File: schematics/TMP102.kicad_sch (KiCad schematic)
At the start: 7 parts, among them J9 Fan_CPU_4pin, U5 TMP102xxDRL

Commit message: Файлы измененный Kicad
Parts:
- C26, R15, R16: now not fitted; now left out of the parts list
- U4: renamed from U5; now not fitted; now left out of the parts list
- renumbered J9 to FAN0, R24 to R0400, R25 to R0401
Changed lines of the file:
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@@
 	(text "Address: 1001000x"
 		(exclude_from_sim no)
-		(at 107.95 105.918 0)
+		(at 102.108 108.204 0)
 		(effects
 			(font
-				(size 1.27 1.27)
+				(size 2.54 2.54)
 			)
 		)
@@
 	(text "Что-то из документации не понятно че там происходит.\nОдни пишут, что на выходе тахометра +7V, другие что 3.3V\nили вообще +12V. Одно понятно. Обычная понижайка справится"
 		(exclude_from_sim no)
-		(at 169.672 117.602 0)
+		(at 154.432 134.62 0)
 		(effects
 			(font
-				(size 1.27 1.27)
+				(size 2.54 2.54)
 			)
 			(justify left)
@@
 		(at 107.95 85.09 0)
 		(unit 1)
-		(exclude_from_sim no)
-		(in_bom yes)
-		(on_board yes)
-		(dnp no)
+		(exclude_from_sim yes)
+		(in_bom no)
+		(on_board no)
+		(dnp yes)
 		(fields_autoplaced yes)
 		(property "Reference" "R15"
@@
 		(at 135.89 101.6 0)
 		(unit 1)
-		(exclude_from_sim no)
-		(in_bom yes)
-		(on_board yes)
-		(dnp no)
-		(property "Reference" "U5"
+		(exclude_from_sim yes)
+		(in_bom no)
+		(on_board no)
+		(dnp yes)
+		(property "Reference" "U4"
 			(at 144.78 89.154 0)
 			(effects
@@
 			(project "MasterBoard"
 				(path "/97e8f341-b455-4614-ab7f-cc310164e7aa/c42b4888-b871-46c0-9d59-6fc9dc24c285"
-					(reference "U5")
+					(reference "U4")
 					(unit 1)
 				)
@@
 		(dnp no)
 		(fields_autoplaced yes)
-		(property "Reference" "R25"
+		(property "Reference" "R0401"
 			(at 199.39 104.1399 0)
 			(effects
@@
 			(project "MasterBoard"
 				(path "/97e8f341-b455-4614-ab7f-cc310164e7aa/c42b4888-b871-46c0-9d59-6fc9dc24c285"
-					(reference "R25")
+					(reference "R0401")
 					(unit 1)
 				)
@@
 		(on_board yes)
 		(dnp no)
-		(property "Reference" "J9"
-			(at 202.438 70.358 90)
+		(property "Reference" "FAN0"
+			(at 199.39 72.136 90)
 			(effects
 				(font
@@
 				)
 				(justify left)
+				(hide yes)
 			)
 		)
@@
 			(project "MasterBoard"
 				(path "/97e8f341-b455-4614-ab7f-cc310164e7aa/c42b4888-b871-46c0-9d59-6fc9dc24c285"
-					(reference "J9")
+					(reference "FAN0")
 					(unit 1)
 				)
@@
 		(dnp no)
 		(fields_autoplaced yes)
-		(property "Reference" "R24"
+		(property "Reference" "R0400"
 			(at 199.39 93.9799 0)
 			(effects
@@
 			(project "MasterBoard"
 				(path "/97e8f341-b455-4614-ab7f-cc310164e7aa/c42b4888-b871-46c0-9d59-6fc9dc24c285"
-					(reference "R24")
+					(reference "R0400")
 					(unit 1)
 				)
@@
 		(at 127 85.09 0)
 		(unit 1)
-		(exclude_from_sim no)
-		(in_bom yes)
-		(on_board yes)
-		(dnp no)
+		(exclude_from_sim yes)
+		(in_bom no)
+		(on_board no)
+		(dnp yes)
 		(fields_autoplaced yes)
 		(property "Reference" "C26"
@@
 		(at 118.11 85.09 0)
 		(unit 1)
-		(exclude_from_sim no)
-		(in_bom yes)
-		(on_board yes)
-		(dnp no)
+		(exclude_from_sim yes)
+		(in_bom no)
+		(on_board no)
+		(dnp yes)
 		(fields_autoplaced yes)
 		(property "Reference" "R16"

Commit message: Прошелся по всей схеме: 1. почистил компоненты; 2. задал посадочные места; 3. Выставил все ссылки на плате в притык, дальнейшее расширение - смена мк
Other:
- company: (none) -> Филимонов и К
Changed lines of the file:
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@@
 	(title_block
 		(date "2025-02-25")
+		(company "Филимонов и К")
 		(comment 1 "TMP102")
 		(comment 2 "Филимонов С.В.")

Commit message: Множественные модификации
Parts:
- renumbered U4 to U3
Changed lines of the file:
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@@
 		(on_board no)
 		(dnp yes)
-		(property "Reference" "U4"
+		(property "Reference" "U3"
 			(at 144.78 89.154 0)
 			(effects
@@
 			(project "MasterBoard"
 				(path "/97e8f341-b455-4614-ab7f-cc310164e7aa/c42b4888-b871-46c0-9d59-6fc9dc24c285"
-					(reference "U4")
+					(reference "U3")
 					(unit 1)
 				)

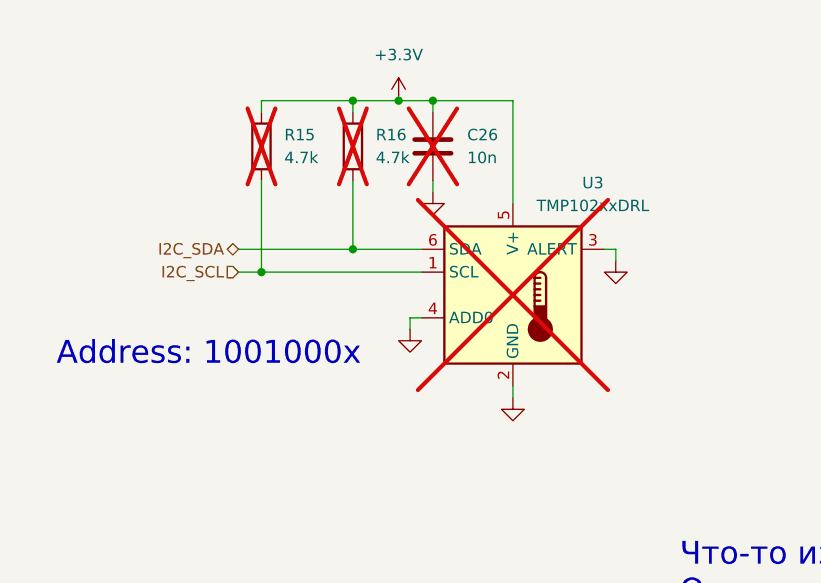
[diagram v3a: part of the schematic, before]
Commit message: Удалил TMP100 - лишний груз был
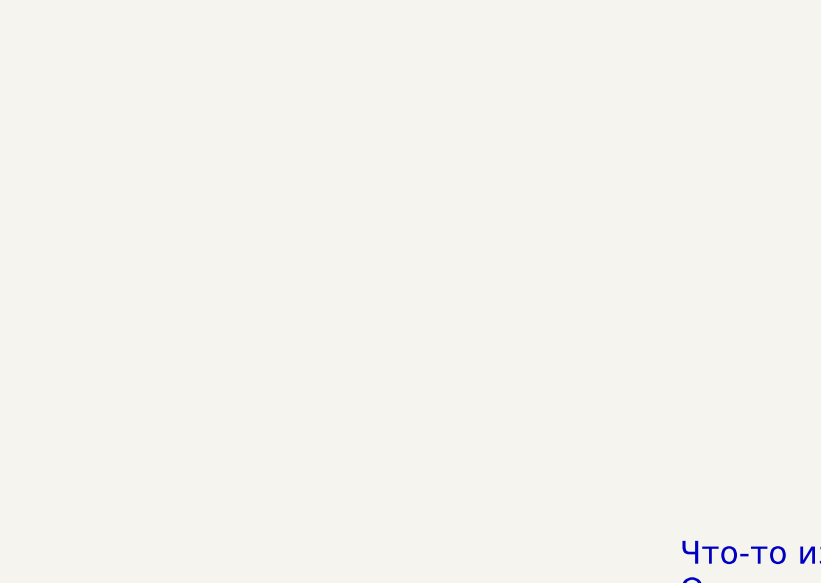
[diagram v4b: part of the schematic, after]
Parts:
- removed C26: 10n, Capacitor_SMD:C_0805_2012Metric, symbol Device:C
- removed R15, R16: 4.7k, Resistor_SMD:R_0805_2012Metric, symbol Device:R
- removed U3: TMP102xxDRL, Package_TO_SOT_SMD:SOT-563, symbol Sensor_Temperature:TMP102xxDRL
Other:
- note removed: "Address: 1001000x"
